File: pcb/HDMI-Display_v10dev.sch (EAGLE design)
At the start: 95 parts, among them IC1 TFP401A-PAD, IC2 24LC02B, IC3 IS31BL3506A-TTLS2, IC4 ATMEGA32U4-MU, IC5 LDO-TS1117-3V3, Q1 16MHz, SW1 SW-TACTILE-TL3315, X1 PASSER-07, X2 PASSER-07, X3 PASSER-07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

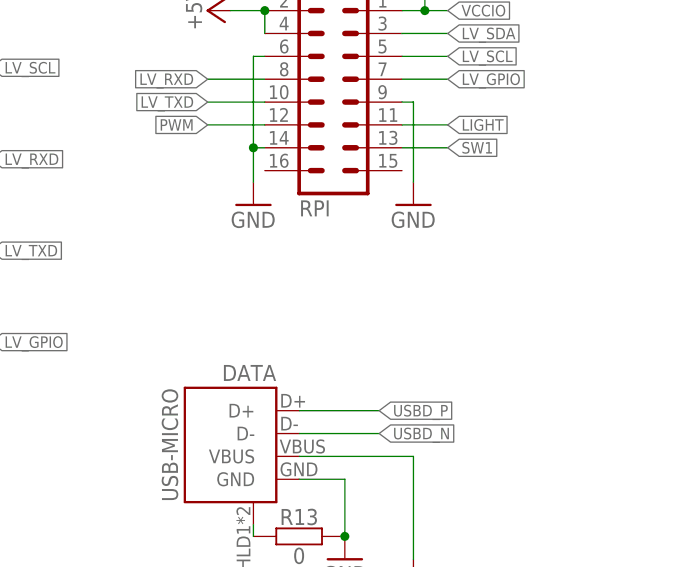
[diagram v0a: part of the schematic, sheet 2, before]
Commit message: updated schematics
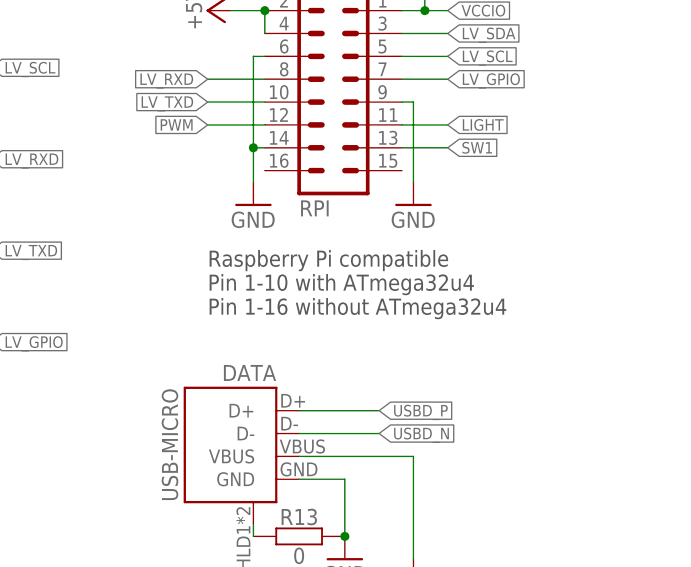
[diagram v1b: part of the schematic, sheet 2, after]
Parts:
- R7B: value 100k -> NM
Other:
- note added: "Raspberry Pi compatible Pin 1-10 with ATmega32u4 Pin 1-16 without ATmega32u4"
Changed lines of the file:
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@@
 <setting verticaltext="up"/>
 </settings>
-<grid distance="0.1" unitdist="inch" unit="inch" style="lines" multiple="1" display="no" altdistance="0.01" altunitdist="inch" altunit="inch"/>
+<grid distance="0.05" unitdist="inch" unit="inch" style="lines" multiple="1" display="yes" altdistance="0.025" altunitdist="inch" altunit="inch"/>
 <layers>
 <layer number="1" name="Top" color="4" fill="1" visible="no" active="no"/>
@@
 <part name="P+1" library="supply1" deviceset="+5V" device=""/>
 <part name="+3V1" library="supply1" deviceset="+3V3" device=""/>
-<part name="R7B" library="we-rcl" deviceset="RESISTOR" device="-R0402" value="100k"/>
+<part name="R7B" library="we-rcl" deviceset="RESISTOR" device="-R0402" value="NM"/>
 <part name="SDA" library="we-rcl" deviceset="JUMPER2" device="" value="JUMPER2"/>
 <part name="SCL" library="we-rcl" deviceset="JUMPER2" device="" value="JUMPER2"/>
@@
 <text x="162.56" y="12.7" size="1.27" layer="95">Based on the work of Hubert Kahlert (HK-Datentechnik)</text>
 <wire x1="222.25" y1="79.375" x2="222.25" y2="77.47" width="0.4064" layer="94"/>
+<text x="199.39" y="116.84" size="1.778" layer="97" align="top-left">Raspberry Pi compatible
+Pin 1-10 with ATmega32u4
+Pin 1-16 without ATmega32u4</text>
 </plain>
 <instances>
@@
 </schematic>
 </drawing>
+<compatibility>
+<note version="6.3" minversion="6.2.2" severity="warning">
+Since Version 6.2.2 text objects can contain more than one line,
+which will not be processed correctly with this version.
+</note>
+</compatibility>
 </eagle>
